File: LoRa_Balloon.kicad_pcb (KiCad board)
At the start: 2 copper layers, 59 parts, among them J1 COAX, J2 Qwicc_6-pin, U1 SKY67013-396LF_CID141, U2 SX1272IMLTRICT-ND_CID104, U3 SKY67013-396LF_CID141, U4 PE4259_CID105, U5 ATMEGA328P-AU, X1 X1E0000210162_CID142, X2 7A-12.000MAAJ-T_CID117

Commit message: PCB finished
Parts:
- added ?: , dtusat:via-0.6mm-0.3mm_drill, F.Cu at (48.2, 19.6)
- added ?: , dtusat:via-0.6mm-0.3mm_drill, F.Cu at (52.7, 43.7)
- added ?: , dtusat:via-0.6mm-0.3mm_drill, F.Cu at (49.2, 21.4)
- added ?: , dtusat:via-0.6mm-0.3mm_drill, F.Cu at (49.2, 22.4)
- added ?: , dtusat:via-0.6mm-0.3mm_drill, F.Cu at (48.7, 23.3)
- added ?: , dtusat:via-0.6mm-0.3mm_drill, F.Cu at (47.7, 23.7)
- added ?: , dtusat:via-0.6mm-0.3mm_drill, F.Cu at (47.4, 24.7)
- added ?: , dtusat:via-0.6mm-0.3mm_drill, F.Cu at (47.5, 25.8)
- added ?: , dtusat:via-0.6mm-0.3mm_drill, F.Cu at (43.7, 20.4)
- added ?: , dtusat:via-0.6mm-0.3mm_drill, F.Cu at (43.7, 21.4)
- added ?: , dtusat:via-0.6mm-0.3mm_drill, F.Cu at (43.7, 22.4)
- added ?: , dtusat:via-0.6mm-0.3mm_drill, F.Cu at (44.2, 23.3)
- added ?: , dtusat:via-0.6mm-0.3mm_drill, F.Cu at (58.7, 44.4)
- added ?: , dtusat:via-0.6mm-0.3mm_drill, F.Cu at (45.2, 23.7)
- added ?: , dtusat:via-0.6mm-0.3mm_drill, F.Cu at (45.4, 24.7)
- added ?: , dtusat:via-0.6mm-0.3mm_drill, F.Cu at (45.4, 25.8)
- added ?: , dtusat:via-0.6mm-0.3mm_drill, F.Cu at (45.3, 46.9)
- added ?: , dtusat:via-0.6mm-0.3mm_drill, F.Cu at (44.2, 46.9)
- added ?: , dtusat:via-0.6mm-0.3mm_drill, F.Cu at (45.3, 44.8)
- added ?: , dtusat:via-0.6mm-0.3mm_drill, F.Cu at (44.2, 45.8)
- added ?: , dtusat:via-0.6mm-0.3mm_drill, F.Cu at (44.2, 44.8)
- added ?: , dtusat:via-0.6mm-0.3mm_drill, F.Cu at (45.3, 45.8)
- added ?: , dtusat:via-0.6mm-0.3mm_drill, F.Cu at (46.3, 44.8)
- added ?: , dtusat:via-0.6mm-0.3mm_drill, F.Cu at (56.3, 28.5)
- added ?: , dtusat:via-0.6mm-0.3mm_drill, F.Cu at (46.3, 45.8)
- added ?: , dtusat:via-0.6mm-0.3mm_drill, F.Cu at (46.3, 46.9)
- added ?: , dtusat:via-0.6mm-0.3mm_drill, F.Cu at (47.4, 46.9)
- added ?: , dtusat:via-0.6mm-0.3mm_drill, F.Cu at (47.4, 45.8)
- added ?: , dtusat:via-0.6mm-0.3mm_drill, F.Cu at (47.4, 44.8)
- added ?: , dtusat:via-0.6mm-0.3mm_drill, F.Cu at (47.4, 43.7)
- added ?: , dtusat:via-0.6mm-0.3mm_drill, F.Cu at (46.3, 43.7)
- added ?: , dtusat:via-0.6mm-0.3mm_drill, F.Cu at (45.3, 43.7)
- added ?: , dtusat:via-0.6mm-0.3mm_drill, F.Cu at (44.2, 43.7)
- added ?: , dtusat:via-0.6mm-0.3mm_drill, F.Cu at (46.6, 41.0)
- added ?: , dtusat:via-0.6mm-0.3mm_drill, F.Cu at (58.9, 28.9)
- added ?: , dtusat:via-0.6mm-0.3mm_drill, F.Cu at (46.8, 40.0)
- added ?: , dtusat:via-0.6mm-0.3mm_drill, F.Cu at (47.8, 39.9)
- added ?: , dtusat:via-0.6mm-0.3mm_drill, F.Cu at (48.8, 40.0)
- added ?: , dtusat:via-0.6mm-0.3mm_drill, F.Cu at (49.8, 40.0)
- added ?: , dtusat:via-0.6mm-0.3mm_drill, F.Cu at (52.9, 40.3)
- added ?: , dtusat:via-0.6mm-0.3mm_drill, F.Cu at (54.7, 39.8)
- added ?: , dtusat:via-0.6mm-0.3mm_drill, F.Cu at (55.7, 39.8)
- added ?: , dtusat:via-0.6mm-0.3mm_drill, F.Cu at (56.0, 38.7)
- added ?: , dtusat:via-0.6mm-0.3mm_drill, F.Cu at (56.0, 37.6)
- added ?: , dtusat:via-0.6mm-0.3mm_drill, F.Cu at (56.0, 36.6)
- added ?: , dtusat:via-0.6mm-0.3mm_drill, F.Cu at (58.2, 31.3)
- added ?: , dtusat:via-0.6mm-0.3mm_drill, F.Cu at (56.8, 35.9)
- added ?: , dtusat:via-0.6mm-0.3mm_drill, F.Cu at (56.8, 34.8)
- added ?: , dtusat:via-0.6mm-0.3mm_drill, F.Cu at (56.0, 34.1)
- added ?: , dtusat:via-0.6mm-0.3mm_drill, F.Cu at (56.0, 33.1)
- added ?: , dtusat:via-0.6mm-0.3mm_drill, F.Cu at (51.9, 32.1)
- added ?: , dtusat:via-0.6mm-0.3mm_drill, F.Cu at (48.9, 31.5)
- added ?: , dtusat:via-0.6mm-0.3mm_drill, F.Cu at (48.0, 30.6)
- added ?: , dtusat:via-0.6mm-0.3mm_drill, F.Cu at (49.9, 32.5)
- added ?: , dtusat:via-0.6mm-0.3mm_drill, F.Cu at (48.5, 32.5)
- added ?: , dtusat:via-0.6mm-0.3mm_drill, F.Cu at (46.9, 34.2)
- added ?: , dtusat:via-0.6mm-0.3mm_drill, F.Cu at (59.4, 33.5)
- added ?: , dtusat:via-0.6mm-0.3mm_drill, F.Cu at (47.9, 34.5)
- added ?: , dtusat:via-0.6mm-0.3mm_drill, F.Cu at (49.0, 34.5)
- added ?: , dtusat:via-0.6mm-0.3mm_drill, F.Cu at (50.0, 34.9)
- added ?: , dtusat:via-0.6mm-0.3mm_drill, F.Cu at (50.9, 35.4)
- added ?: , dtusat:via-0.6mm-0.3mm_drill, F.Cu at (52.0, 35.3)
- added ?: , dtusat:via-0.6mm-0.3mm_drill, F.Cu at (53.1, 35.4)
- added ?: , dtusat:via-0.6mm-0.3mm_drill, F.Cu at (55.1, 32.6)
- added ?: , dtusat:via-0.6mm-0.3mm_drill, F.Cu at (54.0, 35.0)
- added ?: , dtusat:via-0.6mm-0.3mm_drill, F.Cu at (53.9, 36.0)
- added ?: , dtusat:via-0.6mm-0.3mm_drill, F.Cu at (53.9, 37.1)
- added ?: , dtusat:via-0.6mm-0.3mm_drill, F.Cu at (59.0, 37.8)
- added ?: , dtusat:via-0.6mm-0.3mm_drill, F.Cu at (52.8, 37.1)
- added ?: , dtusat:via-0.6mm-0.3mm_drill, F.Cu at (51.7, 37.1)
- added ?: , dtusat:via-0.6mm-0.3mm_drill, F.Cu at (51.1, 38.0)
- added ?: , dtusat:via-0.6mm-0.3mm_drill, F.Cu at (50.1, 37.9)
- added ?: , dtusat:via-0.6mm-0.3mm_drill, F.Cu at (49.0, 37.9)
- added ?: , dtusat:via-0.6mm-0.3mm_drill, F.Cu at (48.3, 37.2)
- added ?: , dtusat:via-0.6mm-0.3mm_drill, F.Cu at (47.3, 37.2)
- added ?: , dtusat:via-0.6mm-0.3mm_drill, F.Cu at (45.9, 37.5)
- added ?: , dtusat:via-0.6mm-0.3mm_drill, F.Cu at (46.8, 38.0)
- added ?: , dtusat:via-0.6mm-0.3mm_drill, F.Cu at (45.5, 38.4)
- added ?: , dtusat:via-0.6mm-0.3mm_drill, F.Cu at (59.1, 40.2)
- added ?: , dtusat:via-0.6mm-0.3mm_drill, F.Cu at (45.5, 36.6)
- added ?: , dtusat:via-0.6mm-0.3mm_drill, F.Cu at (45.5, 35.6)
- added ?: , dtusat:via-0.6mm-0.3mm_drill, F.Cu at (45.5, 34.5)
- added ?: , dtusat:via-0.6mm-0.3mm_drill, F.Cu at (46.1, 33.7)
- added ?: , dtusat:via-0.6mm-0.3mm_drill, F.Cu at (46.1, 32.6)
- added ?: , dtusat:via-0.6mm-0.3mm_drill, F.Cu at (45.9, 31.6)
- added ?: , dtusat:via-0.6mm-0.3mm_drill, F.Cu at (43.0, 38.5)
- added ?: , dtusat:via-0.6mm-0.3mm_drill, F.Cu at (43.5, 37.6)
- added ?: , dtusat:via-0.6mm-0.3mm_drill, F.Cu at (43.4, 36.6)
- added ?: , dtusat:via-0.6mm-0.3mm_drill, F.Cu at (43.0, 35.7)
- added ?: , dtusat:via-0.6mm-0.3mm_drill, F.Cu at (41.0, 38.4)
- added ?: , dtusat:via-0.6mm-0.3mm_drill, F.Cu at (42.7, 34.7)
- added ?: , dtusat:via-0.6mm-0.3mm_drill, F.Cu at (43.0, 33.7)
- added ?: , dtusat:via-0.6mm-0.3mm_drill, F.Cu at (43.0, 32.7)
- added ?: , dtusat:via-0.6mm-0.3mm_drill, F.Cu at (42.7, 31.7)
- added ?: , dtusat:via-0.6mm-0.3mm_drill, F.Cu at (42.9, 30.8)
- added ?: , dtusat:via-0.6mm-0.3mm_drill, F.Cu at (43.9, 30.6)
- added ?: , dtusat:via-0.6mm-0.3mm_drill, F.Cu at (44.8, 30.2)
- added ?: , dtusat:via-0.6mm-0.3mm_drill, F.Cu at (39.1, 37.9)
- added ?: , dtusat:via-0.6mm-0.3mm_drill, F.Cu at (47.1, 19.6)
- added ?: , dtusat:via-0.6mm-0.3mm_drill, F.Cu at (38.9, 32.7)
- added ?: , dtusat:via-0.6mm-0.3mm_drill, F.Cu at (40.9, 33.7)
- added ?: , dtusat:via-0.6mm-0.3mm_drill, F.Cu at (41.5, 28.5)
- added ?: , dtusat:via-0.6mm-0.3mm_drill, F.Cu at (41.2, 36.6)
- added ?: , dtusat:via-0.6mm-0.3mm_drill, F.Cu at (40.5, 31.0)
- added ?: , dtusat:via-0.6mm-0.3mm_drill, F.Cu at (39.1, 35.3)
- added ?: , dtusat:via-0.6mm-0.3mm_drill, F.Cu at (39.5, 28.7)
- added ?: , dtusat:via-0.6mm-0.3mm_drill, F.Cu at (48.2, 51.8)
- added ?: , dtusat:via-0.6mm-0.3mm_drill, F.Cu at (50.0, 51.8)
- added ?: , dtusat:via-0.6mm-0.3mm_drill, F.Cu at (51.0, 51.8)
- added ?: , dtusat:via-0.6mm-0.3mm_drill, F.Cu at (45.9, 19.6)
- added ?: , dtusat:via-0.6mm-0.3mm_drill, F.Cu at (54.6, 51.8)
- added ?: , dtusat:via-0.6mm-0.3mm_drill, F.Cu at (53.5, 51.8)
- added ?: , dtusat:via-0.6mm-0.3mm_drill, F.Cu at (55.7, 51.8)
- added ?: , dtusat:via-0.6mm-0.3mm_drill, F.Cu at (56.8, 51.8)
- added ?: , dtusat:via-0.6mm-0.3mm_drill, F.Cu at (58.7, 51.7)
- added ?: , dtusat:via-0.6mm-0.3mm_drill, F.Cu at (59.8, 51.7)
- added ?: , dtusat:via-0.6mm-0.3mm_drill, F.Cu at (60.9, 51.7)
- added ?: , dtusat:via-0.6mm-0.3mm_drill, F.Cu at (60.9, 50.6)
- added ?: , dtusat:via-0.6mm-0.3mm_drill, F.Cu at (61.0, 44.1)
- added ?: , dtusat:via-0.6mm-0.3mm_drill, F.Cu at (60.9, 47.4)
- added ?: , dtusat:via-0.6mm-0.3mm_drill, F.Cu at (44.7, 19.7)
- added ?: , dtusat:via-0.6mm-0.3mm_drill, F.Cu at (61.0, 46.3)
- added ?: , dtusat:via-0.6mm-0.3mm_drill, F.Cu at (60.9, 48.5)
- added ?: , dtusat:via-0.6mm-0.3mm_drill, F.Cu at (60.9, 49.5)
- added ?: , dtusat:via-0.6mm-0.3mm_drill, F.Cu at (60.9, 45.2)
- added ?: , dtusat:via-0.6mm-0.3mm_drill, F.Cu at (57.5, 25.8)
- added ?: , dtusat:via-0.6mm-0.3mm_drill, F.Cu at (60.8, 25.8)
- added ?: , dtusat:via-0.6mm-0.3mm_drill, F.Cu at (59.7, 25.8)
- added ?: , dtusat:via-0.6mm-0.3mm_drill, F.Cu at (61.0, 43.0)
- added ?: , dtusat:via-0.6mm-0.3mm_drill, F.Cu at (58.6, 25.8)
- added ?: , dtusat:via-0.6mm-0.3mm_drill, F.Cu at (62.0, 25.8)
- added ?: , dtusat:via-0.6mm-0.3mm_drill, F.Cu at (54.2, 49.8)
- added ?: , dtusat:via-0.6mm-0.3mm_drill, F.Cu at (60.9, 41.3)
- added ?: , dtusat:via-0.6mm-0.3mm_drill, F.Cu at (60.9, 40.0)
- added ?: , dtusat:via-0.6mm-0.3mm_drill, F.Cu at (51.9, 25.8)
- added ?: , dtusat:via-0.6mm-0.3mm_drill, F.Cu at (50.8, 25.8)
- added ?: , dtusat:via-0.6mm-0.3mm_drill, F.Cu at (48.5, 25.8)
- added ?: , dtusat:via-0.6mm-0.3mm_drill, F.Cu at (49.6, 25.8)
- added ?: , dtusat:via-0.6mm-0.3mm_drill, F.Cu at (53.0, 25.8)
- added ?: , dtusat:via-0.6mm-0.3mm_drill, F.Cu at (54.1, 25.8)
- added ?: , dtusat:via-0.6mm-0.3mm_drill, F.Cu at (55.3, 25.8)
- added ?: , dtusat:via-0.6mm-0.3mm_drill, F.Cu at (56.4, 25.8)
- added ?: , dtusat:via-0.6mm-0.3mm_drill, F.Cu at (58.1, 49.2)
- added ?: , dtusat:via-0.6mm-0.3mm_drill, F.Cu at (60.9, 33.7)
- added ?: , dtusat:via-0.6mm-0.3mm_drill, F.Cu at (60.9, 38.7)
- added ?: , dtusat:via-0.6mm-0.3mm_drill, F.Cu at (60.9, 35.9)
- added ?: , dtusat:via-0.6mm-0.3mm_drill, F.Cu at (60.9, 37.3)
- added ?: , dtusat:via-0.6mm-0.3mm_drill, F.Cu at (60.9, 34.8)
- added ?: , dtusat:via-0.6mm-0.3mm_drill, F.Cu at (61.0, 29.3)
- added ?: , dtusat:via-0.6mm-0.3mm_drill, F.Cu at (61.0, 28.2)
- added ?: , dtusat:via-0.6mm-0.3mm_drill, F.Cu at (61.0, 31.5)
- added ?: , dtusat:via-0.6mm-0.3mm_drill, F.Cu at (61.0, 30.4)
- added ?: , dtusat:via-0.6mm-0.3mm_drill, F.Cu at (61.0, 32.6)
- added ?: , dtusat:via-0.6mm-0.3mm_drill, F.Cu at (58.6, 46.6)
- added ?: , dtusat:via-0.6mm-0.3mm_drill, F.Cu at (43.0, 49.4)
- added ?: , dtusat:via-0.6mm-0.3mm_drill, F.Cu at (45.0, 51.0)
- added ?: , dtusat:via-0.6mm-0.3mm_drill, F.Cu at (44.1, 51.8)
- added ?: , dtusat:via-0.6mm-0.3mm_drill, F.Cu at (38.6, 51.2)
- added ?: , dtusat:via-0.6mm-0.3mm_drill, F.Cu at (37.5, 51.7)
- added ?: , dtusat:via-0.6mm-0.3mm_drill, F.Cu at (37.5, 49.5)
- added ?: , dtusat:via-0.6mm-0.3mm_drill, F.Cu at (37.5, 50.6)
- added ?: , dtusat:via-0.6mm-0.3mm_drill, F.Cu at (37.5, 29.4)
- added ?: , dtusat:via-0.6mm-0.3mm_drill, F.Cu at (37.5, 28.3)
- added ?: , dtusat:via-0.6mm-0.3mm_drill, F.Cu at (37.5, 44.3)
- added ?: , dtusat:via-0.6mm-0.3mm_drill, F.Cu at (55.1, 47.0)
- added ?: , dtusat:via-0.6mm-0.3mm_drill, F.Cu at (37.5, 41.9)
- added ?: , dtusat:via-0.6mm-0.3mm_drill, F.Cu at (37.5, 40.8)
- added ?: , dtusat:via-0.6mm-0.3mm_drill, F.Cu at (37.5, 43.3)
- added ?: , dtusat:via-0.6mm-0.3mm_drill, F.Cu at (37.5, 39.7)
- added ?: , dtusat:via-0.6mm-0.3mm_drill, F.Cu at (37.5, 36.4)
- added ?: , dtusat:via-0.6mm-0.3mm_drill, F.Cu at (37.5, 35.3)
- added ?: , dtusat:via-0.6mm-0.3mm_drill, F.Cu at (37.5, 38.6)
- added ?: , dtusat:via-0.6mm-0.3mm_drill, F.Cu at (37.5, 37.5)
- added ?: , dtusat:via-0.6mm-0.3mm_drill, F.Cu at (37.5, 30.9)
- added ?: , dtusat:via-0.6mm-0.3mm_drill, F.Cu at (37.5, 32.0)
- added ?: , dtusat:via-0.6mm-0.3mm_drill, F.Cu at (55.7, 44.3)
- added ?: , dtusat:via-0.6mm-0.3mm_drill, F.Cu at (37.5, 34.2)
- added ?: , dtusat:via-0.6mm-0.3mm_drill, F.Cu at (37.5, 33.1)
- added ?: , dtusat:via-0.6mm-0.3mm_drill, F.Cu at (37.6, 25.8)
- added ?: , dtusat:via-0.6mm-0.3mm_drill, F.Cu at (38.7, 25.8)
- added ?: , dtusat:via-0.6mm-0.3mm_drill, F.Cu at (39.8, 25.8)
- added ?: , dtusat:via-0.6mm-0.3mm_drill, F.Cu at (40.9, 25.8)
- added ?: , dtusat:via-0.6mm-0.3mm_drill, F.Cu at (42.1, 25.8)
- added ?: , dtusat:via-0.6mm-0.3mm_drill, F.Cu at (43.1, 25.8)
- added ?: , dtusat:via-0.6mm-0.3mm_drill, F.Cu at (44.3, 25.8)
- added ?: , dtusat:via-0.6mm-0.3mm_drill, F.Cu at (49.2, 20.3)
- L2: value L_0603_33nH_CID3014 -> L_0402_33nH_CID3034; footprint dtusat:L0603 -> dtusat:L0402
- moved L9 126.5 mm to (44.0, 33.2), turned to 270 degrees
- moved L8 124.3 mm to (44.5, 36.2), turned to 270 degrees
- moved R4 123.3 mm to (36.6, 62.3), turned to 180 degrees
- moved L2 120.7 mm to (43.4, 40.8), turned to 270 degrees
- moved L4 120.5 mm to (44.5, 40.8), turned to 270 degrees
- moved L6 120.3 mm to (46.1, 39.3), turned to 225 degrees
- moved R2 118.0 mm to (41.5, 48.7), turned to 90 degrees
- moved L7 116.5 mm to (50.9, 39.4), turned to 90 degrees
- moved C33 115.5 mm to (39.2, 68.7), turned to 270 degrees
- moved L1 114.9 mm to (49.5, 33.5), turned to 180 degrees
- moved C28 112.9 mm to (44.1, 31.6), turned to 180 degrees
- moved C27 112.5 mm to (44.2, 28.4), turned to 180 degrees
- moved C29 111.7 mm to (48.6, 28.4)
- moved L3 111.5 mm to (53.9, 33.0), turned to 270 degrees
- moved L5 111.0 mm to (55.0, 38.5), turned to 90 degrees
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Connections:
- C1 pad 2: Net-(C1-Pad2) -> GND
- C10 pad 1: Net-(C10-Pad1) -> +3V3
- C2 pad 1: Net-(C2-Pad1) -> +3V3
- J2 pad 3: Net-(J2-Pad3) -> /Reset
- L2 pad 2: Net-(C7-Pad1) -> Net-(L2-Pad2)
- R2 pad 2: /Reset_SX -> /RXTX_SW
- U2 pad 1: Net-(C2-Pad1) -> +3V3
- U2 pad 15: Net-(C10-Pad1) -> +3V3
- U2 pad 6: /Reset_SX -> /RXTX_SW
- U5 pad 32: /ResetSX -> /RXTX_SW
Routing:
- net +3V3: track 0.00 -> 174.2 mm, vias 0 -> 9
- net /RXTX_SW: track 0.00 -> 57.6 mm, vias 0 -> 8
- net /RF_CS: track 0.00 -> 26.1 mm
- net /MOSI: track 0.00 -> 19.7 mm
- net /DIO0: track 0.00 -> 18.2 mm
- net /DIO1: track 0.00 -> 17.4 mm
- net /MISO: track 0.00 -> 17.1 mm
- net /DIO2: track 0.00 -> 16.6 mm
- net /Reset: track 0.00 -> 16.1 mm, vias 0 -> 2
- net /SCK: track 0.00 -> 15.5 mm
- net /DIO3: track 0.00 -> 15.4 mm
- net /DIO4: track 0.00 -> 13.2 mm
- net /DIO5: track 0.00 -> 12.8 mm
- net /RX: track 0.00 -> 10.5 mm
- net /TX: track 0.00 -> 9.71 mm
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- added copper zone on B.Cu, net GND
- added copper zone on F.Cu, net GND
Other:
- board outline added: 30 x 56 mm

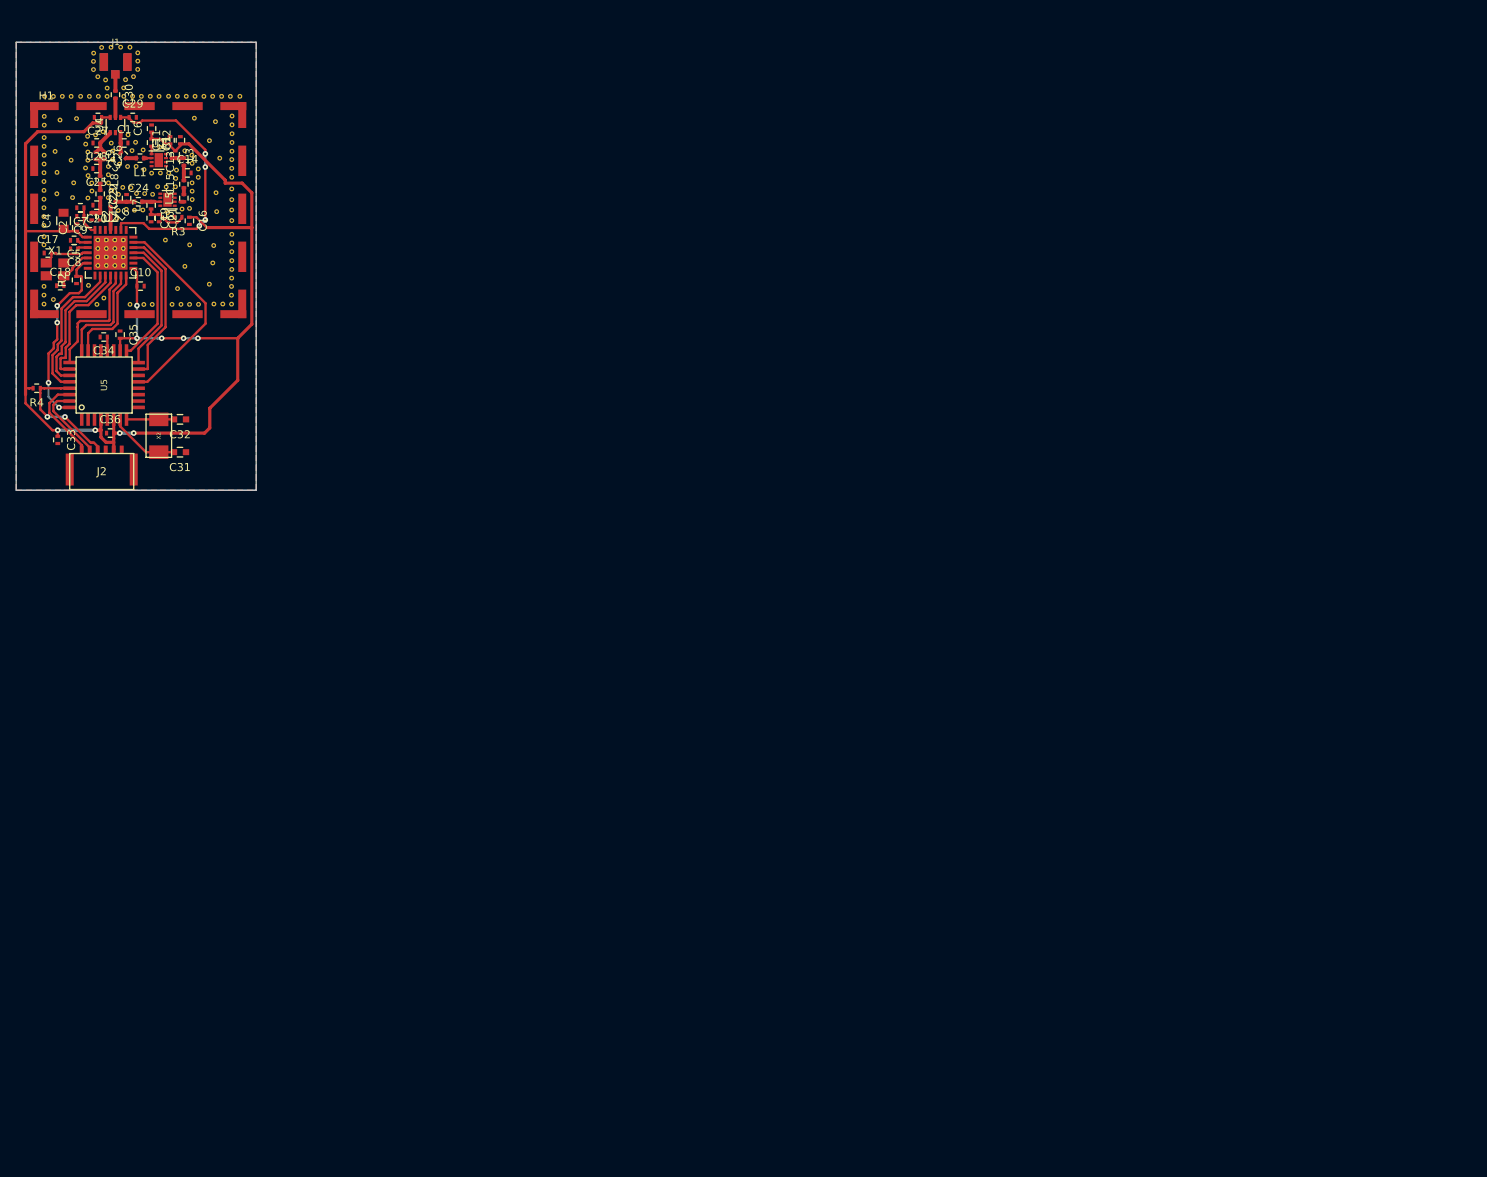
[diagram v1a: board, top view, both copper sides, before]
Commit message: Rearranged component labels
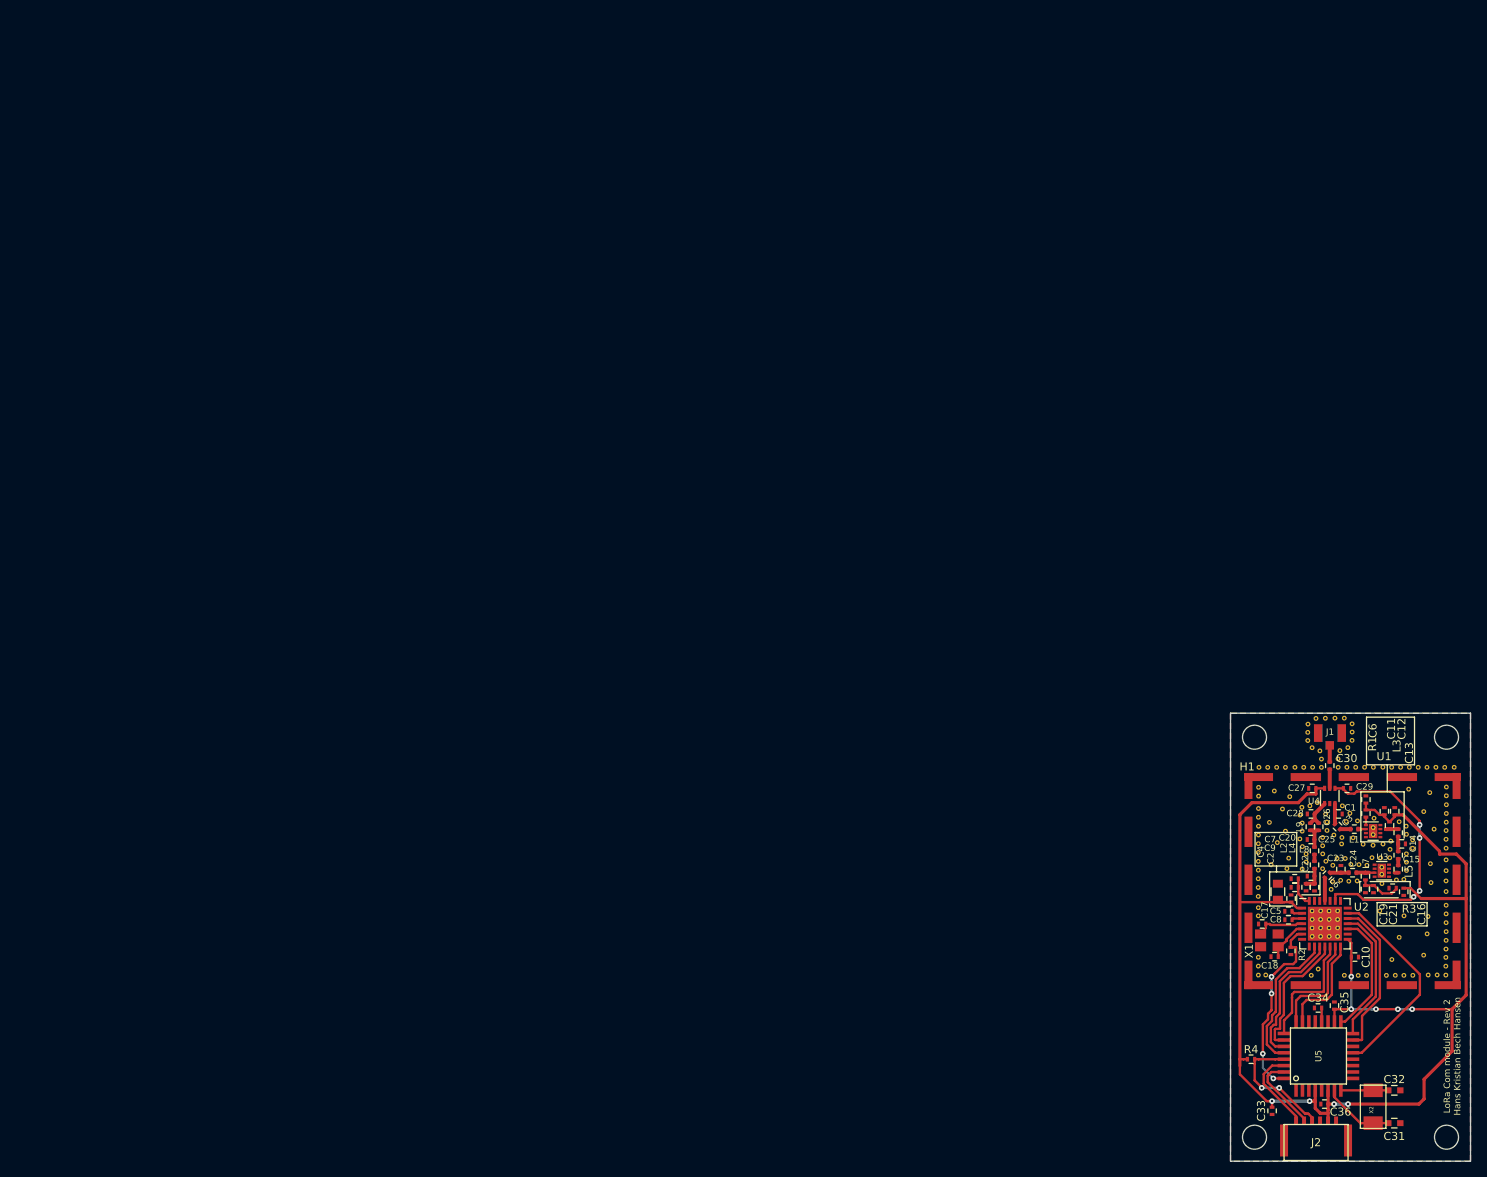
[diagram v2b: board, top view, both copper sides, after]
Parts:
- removed the ? at (43.0, 49.4)
- added ?: , dtusat:via-0.6mm-0.3mm_drill, F.Cu at (204.7, 123.0)
- added ?: , dtusat:via-0.6mm-0.3mm_drill, F.Cu at (204.7, 122.1)
- added ?: , dtusat:via-0.6mm-0.3mm_drill, F.Cu at (203.6, 118.0)
- added ?: , dtusat:via-0.6mm-0.3mm_drill, F.Cu at (203.6, 117.2)
- moved ? 174.0 mm to (191.6, 119.0)
- moved ? 173.8 mm to (193.1, 121.0)
- moved ? 173.7 mm to (193.2, 113.3)
- moved ? 173.5 mm to (190.2, 135.6)
- moved C31 173.4 mm to (206.3, 154.1)
- moved C36 173.4 mm to (197.5, 151.7)
- moved ? 173.4 mm to (209.9, 133.1)
- moved ? 173.4 mm to (194.9, 109.6)
- moved ? 173.4 mm to (196.1, 109.6)
- moved ? 173.4 mm to (201.0, 104.2)
- moved ? 173.4 mm to (201.0, 105.2)
- moved ? 173.4 mm to (201.0, 106.3)
- moved ? 173.4 mm to (200.5, 107.2)
- moved ? 173.4 mm to (199.5, 107.5)
- moved ? 173.4 mm to (199.2, 108.6)
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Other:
- outline, holes or cut-outs redrawn
- board text added: "LoRa Com module - Rev 2 Hans Kristian Bech Hansen"
